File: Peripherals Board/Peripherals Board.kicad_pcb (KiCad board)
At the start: 2 copper layers, 86.6 x 62.5 mm, 38 parts

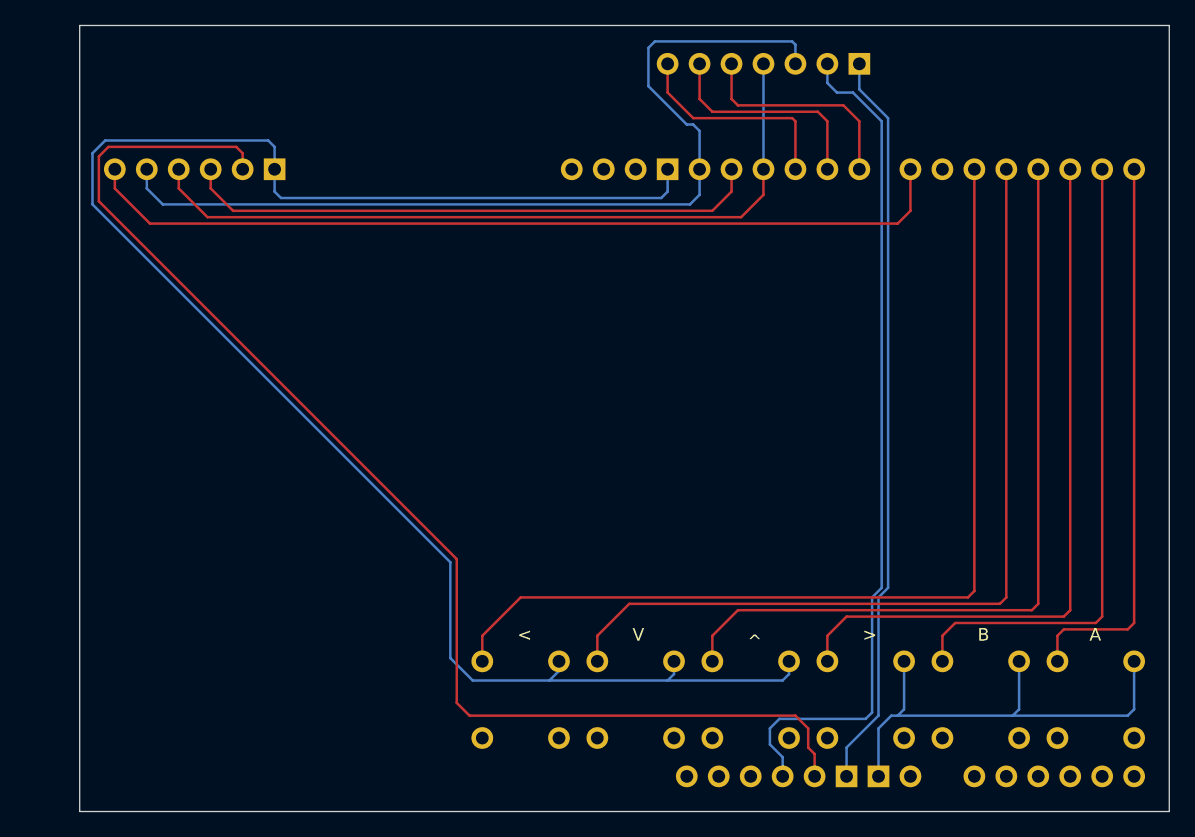
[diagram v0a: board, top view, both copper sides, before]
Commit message: pushbuttons were too far apart, made them 5.08mm instead of ~6mm
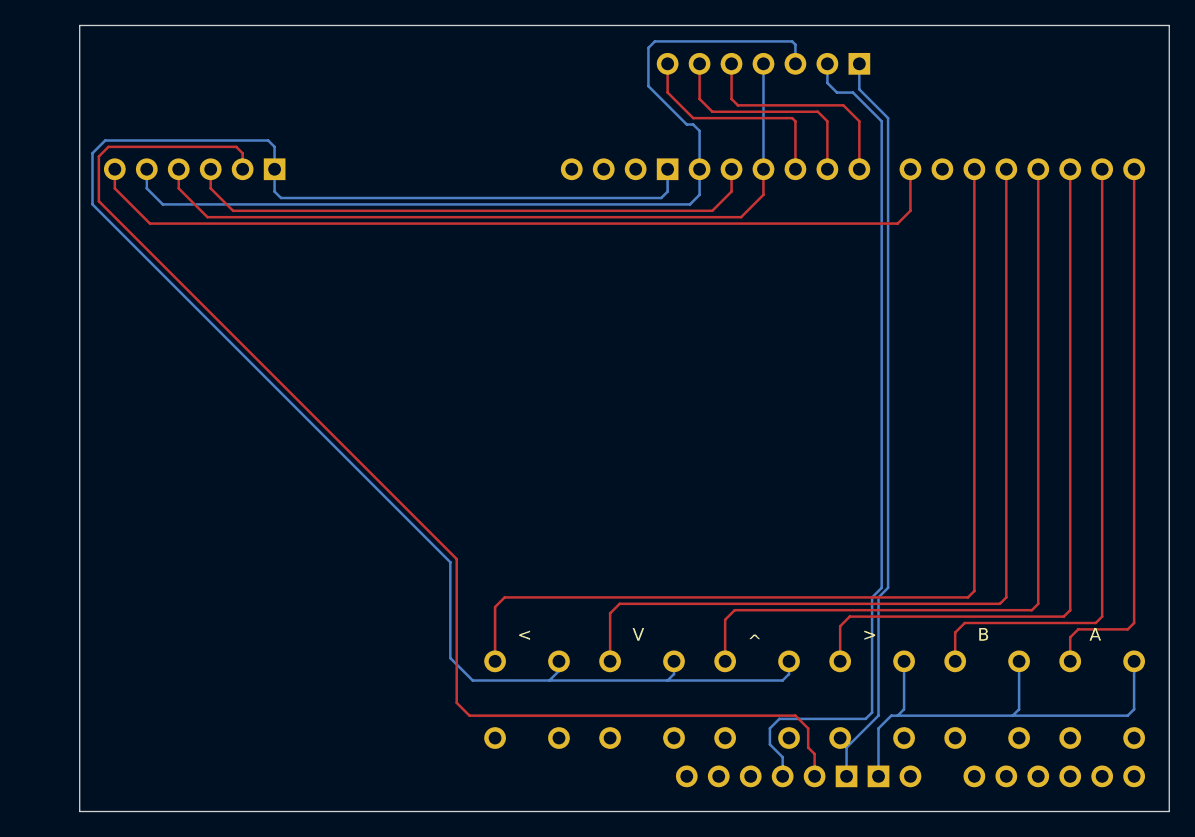
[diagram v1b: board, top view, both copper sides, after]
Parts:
- moved ? 1.02 mm to (166.1, 117.9)
- moved ? 1.02 mm to (166.1, 124.0)
- moved ? 1.02 mm to (157.0, 117.9)
- moved ? 1.02 mm to (157.0, 124.0)
- moved ? 1.02 mm to (129.5, 124.0)
- moved ? 1.02 mm to (147.8, 124.0)
- moved ? 1.02 mm to (138.7, 117.9)
- moved ? 1.02 mm to (147.8, 117.9)
- moved ? 1.02 mm to (129.5, 117.9)
- moved ? 1.02 mm to (175.3, 124.0)
- moved ? 1.02 mm to (138.7, 124.0)
- moved ? 1.02 mm to (175.3, 117.9)
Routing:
- net (no net): track 1065.7 -> 1063.2 mm

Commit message: hw i2c fixed and 0.4 MTT PCB
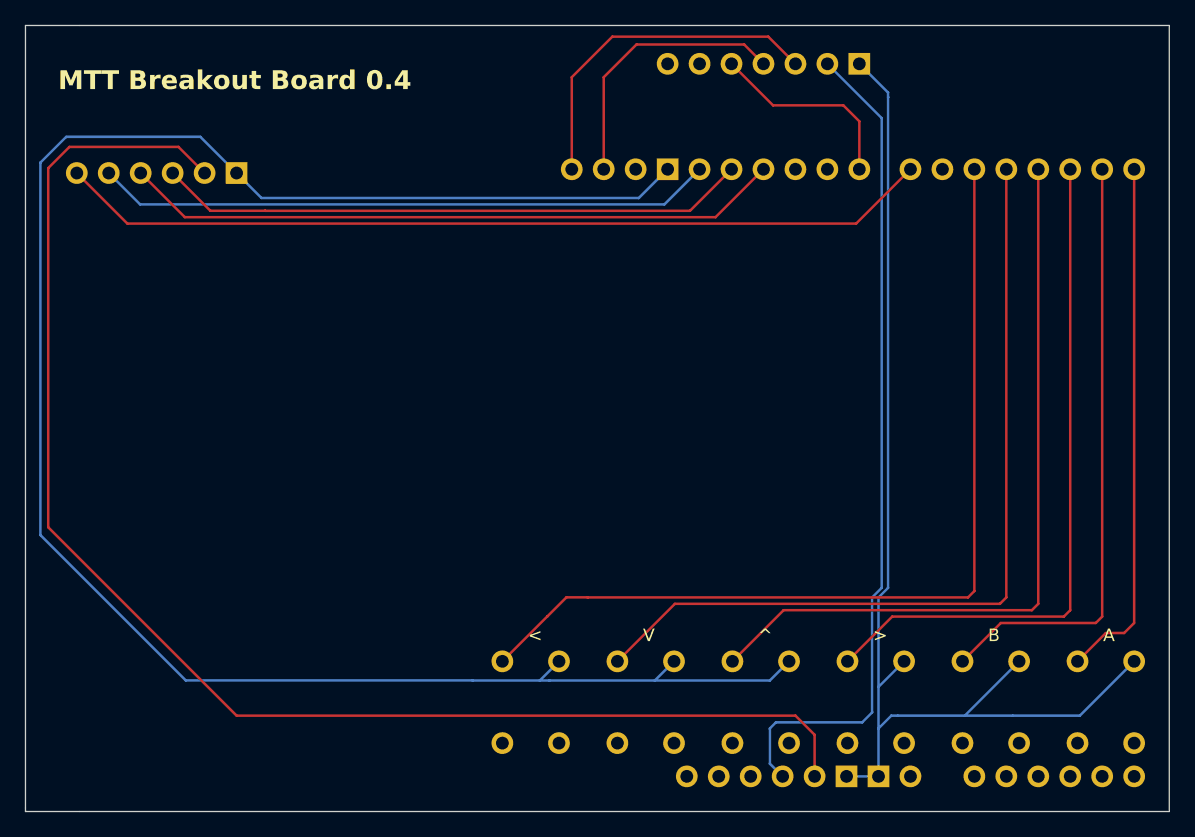
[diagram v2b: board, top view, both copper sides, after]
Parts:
- moved ? 3.04 mm to (103.9, 79.0)
- moved ? 3.04 mm to (101.4, 79.0)
- moved ? 3.04 mm to (98.8, 79.0)
- moved ? 3.04 mm to (109.0, 79.0)
- moved ? 3.04 mm to (106.5, 79.0)
- moved ? 3.04 mm to (96.3, 79.0)
- moved ? 0.71 mm to (130.1, 124.4)
- moved ? 0.71 mm to (175.8, 124.4)
- moved ? 0.71 mm to (139.3, 124.4)
- moved ? 0.71 mm to (166.7, 124.4)
- moved ? 0.71 mm to (148.4, 124.4)
- moved ? 0.71 mm to (157.6, 124.4)
- moved ? 0.58 mm to (139.3, 117.9)
- moved ? 0.58 mm to (130.1, 117.9)
- moved ? 0.58 mm to (175.8, 117.9)
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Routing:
- net (no net): track 1063.2 -> 1053.8 mm
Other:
- board size 86.6 x 62.5 mm -> 90.9 x 62.5 mm
- board text added: "MTT Breakout Board 0.4"
